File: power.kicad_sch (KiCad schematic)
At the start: 28 parts, among them J3 USB_C_Receptacle_Molex, U11 TPD1E05U06DPY, U4 TPS7A5201QRGRRQ1, U6 TPS7A5201QRGRRQ1

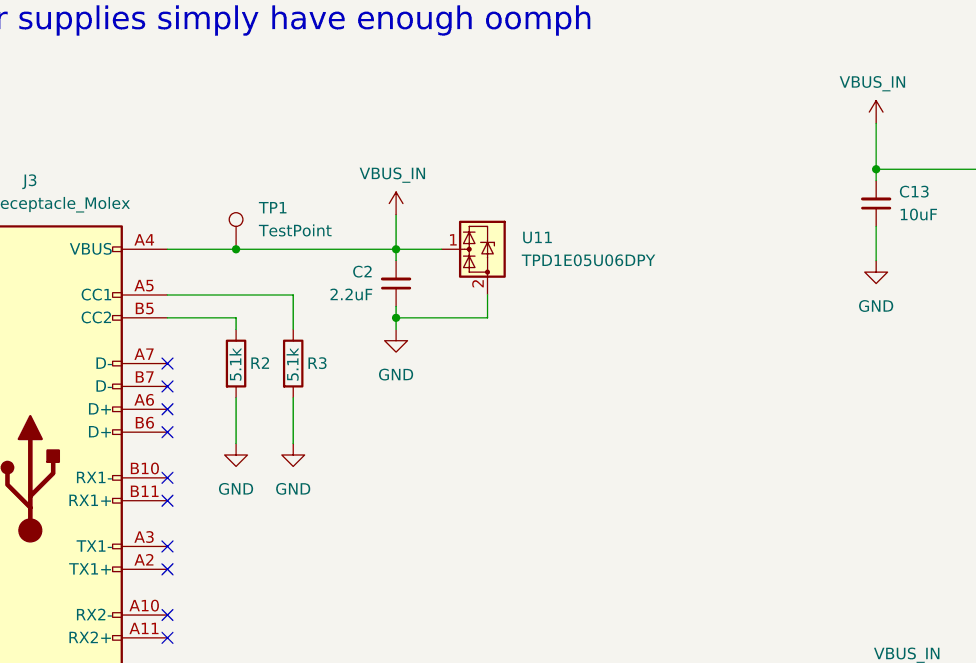
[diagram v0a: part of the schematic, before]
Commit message: Start wiring up Pi Pico
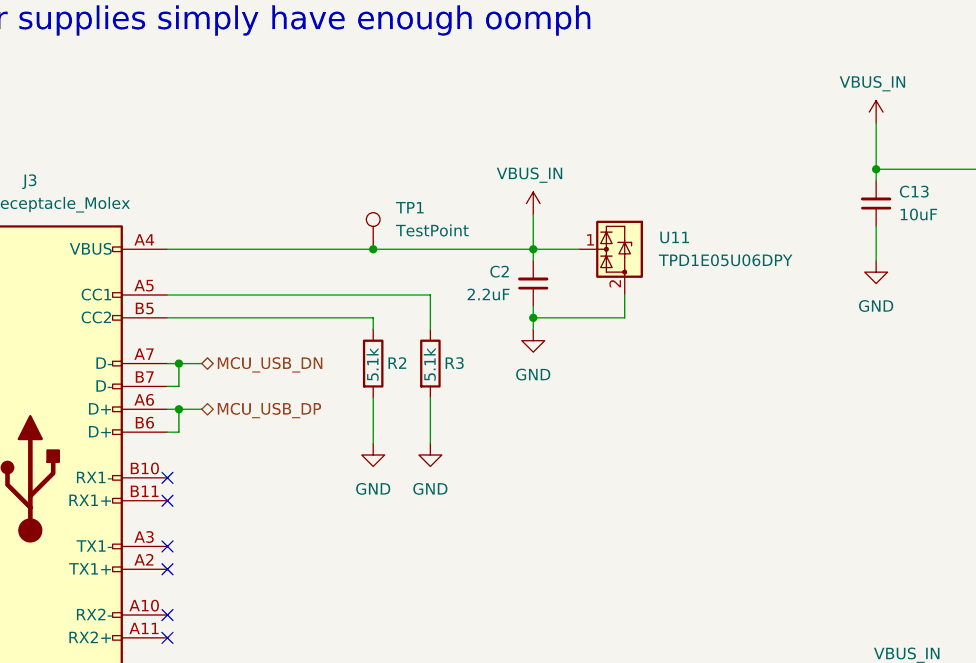
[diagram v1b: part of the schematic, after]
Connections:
- net MCU_USB_DP: now reaches J3.A6 (D+)
- net MCU_USB_DP: now also J3.B6 (D+)
- net MCU_USB_DN: now reaches J3.A7 (D-)
- net MCU_USB_DN: now also J3.B7 (D-)
- no-connect marks 16 -> 12
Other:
- moved on the sheet: C2, R2, R3, TP1, U11

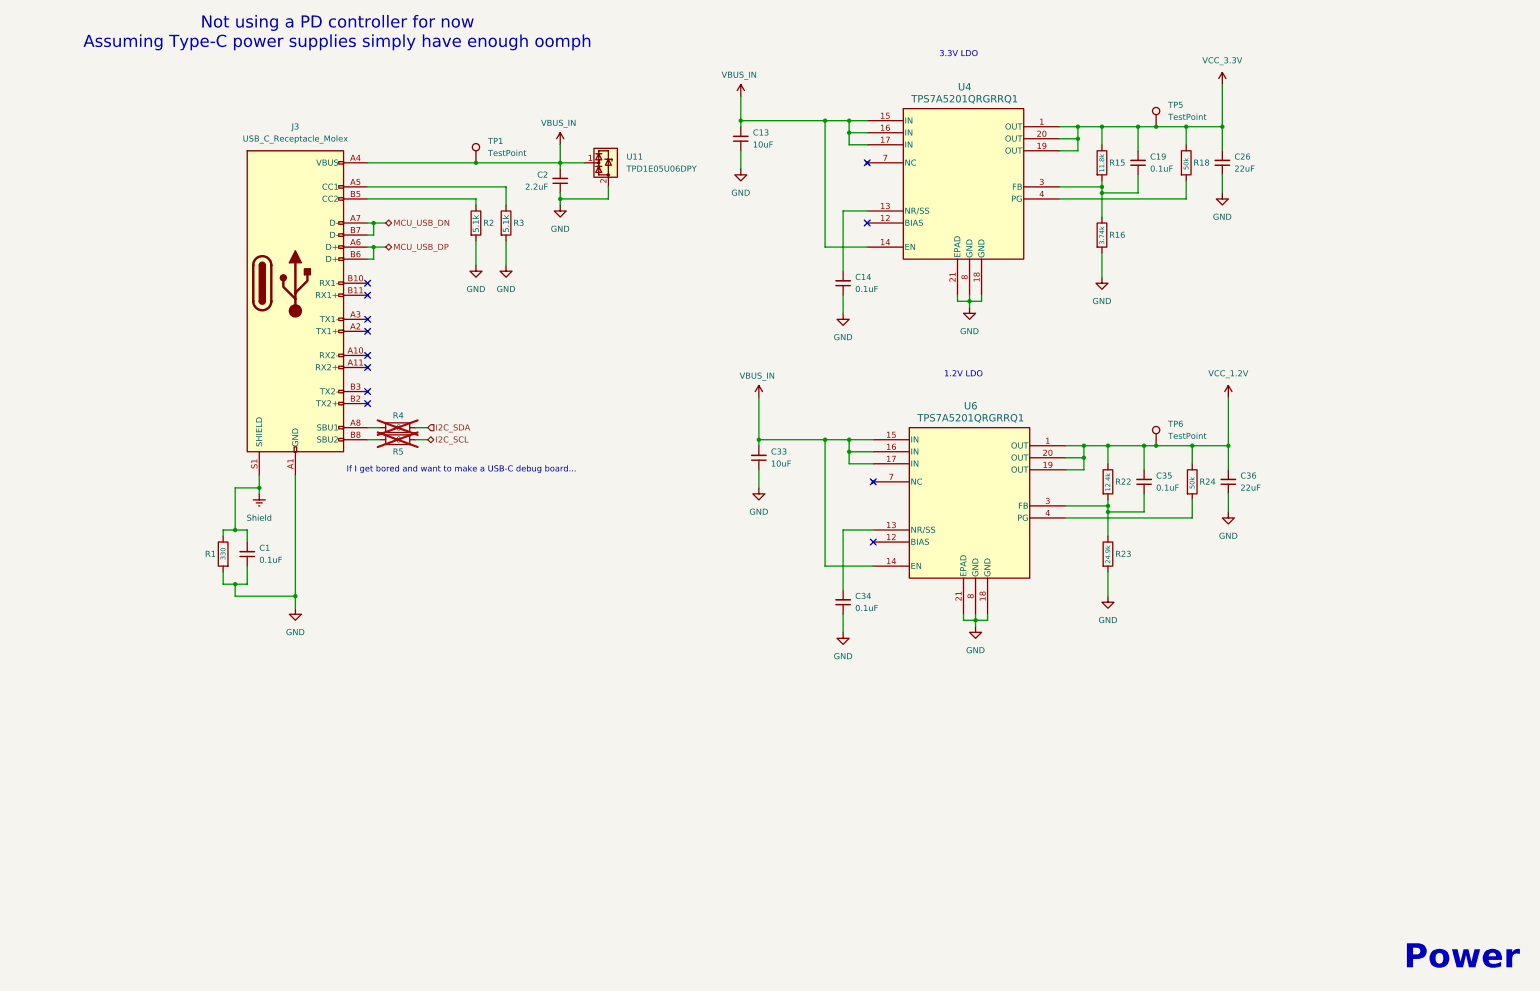
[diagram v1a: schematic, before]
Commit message: Wire up more of the Pico
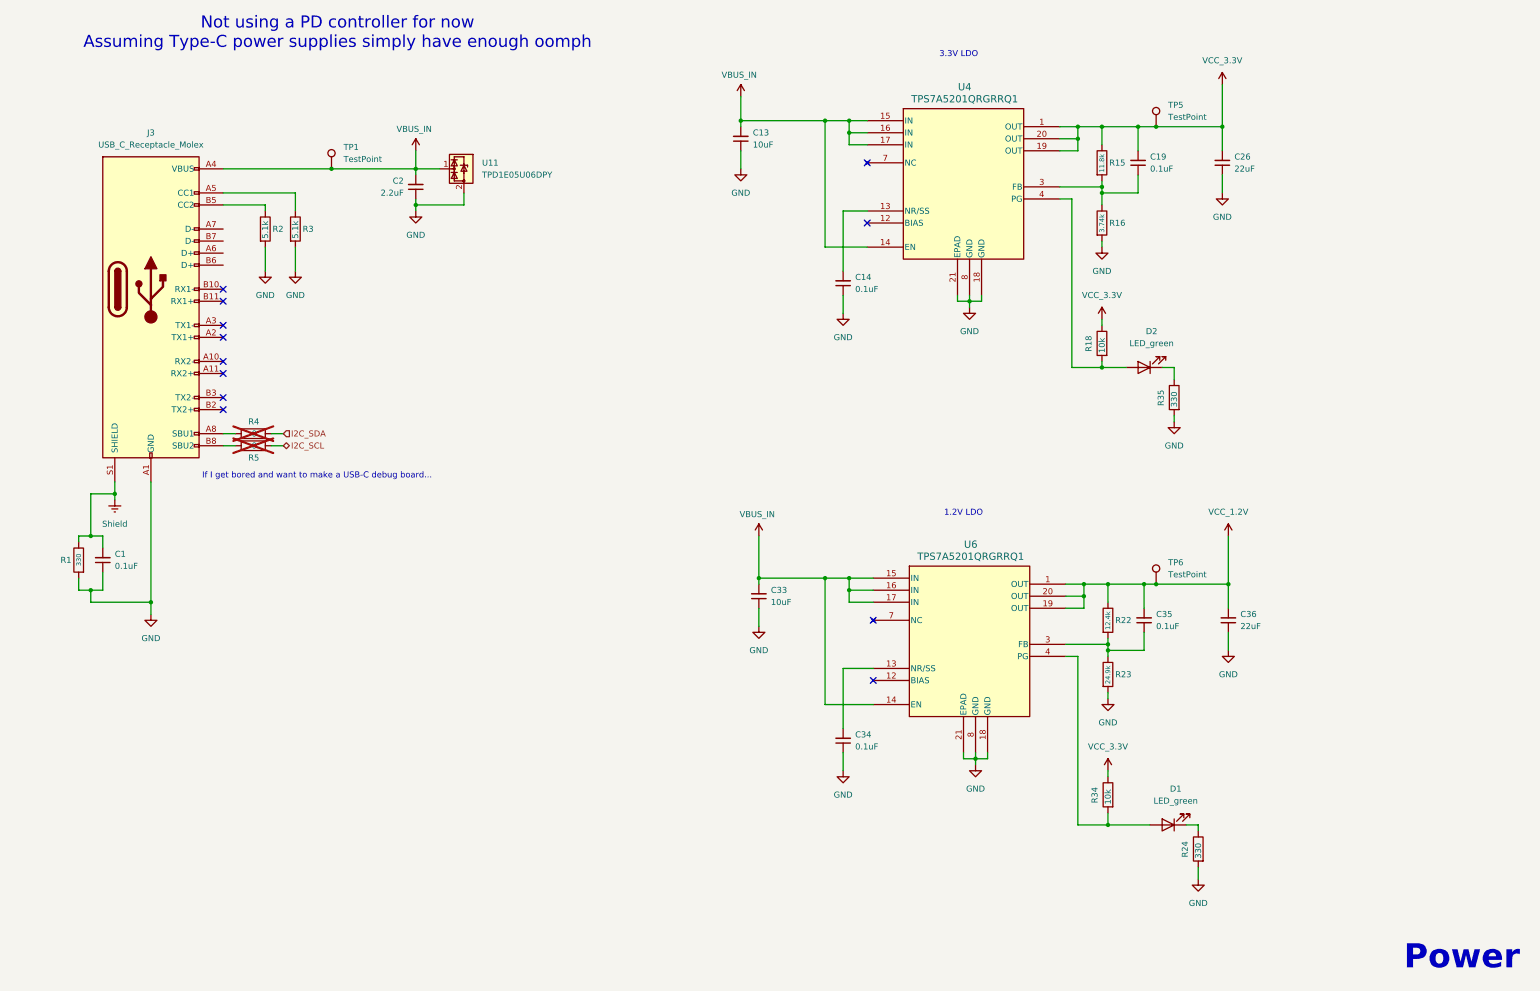
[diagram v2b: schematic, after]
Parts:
- added D1, D2: LED_green, LED_SMD:LED_0603_1608Metric, symbol hubble:LED_green
- added R34: 10k, Resistor_SMD:R_0603_1608Metric, symbol Device:R
- added R35: 330, Resistor_SMD:R_0603_1608Metric, symbol Device:R
- R18: value 50k -> 10k
- R24: value 50k -> 330
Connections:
- net GND: now also R24.2, R35.2
- net VCC_1.2V: no longer R24.1
- net VCC_3.3V: now also R34.1
- net at R18.2, U4.4 (PG): now also D2.2 (A)
- net at U6.4 (PG): now also D1.2 (A), R34.2; no longer R24.2
- net MCU_USB_DN: no longer names the net of J3.A7 (D-)
- net MCU_USB_DN: no longer J3.B7 (D-)
- net MCU_USB_DP: no longer names the net of J3.A6 (D+)
- net MCU_USB_DP: no longer J3.B6 (D+)
- new net: D1.1 (K), R24.1
- new net: D2.1 (K), R35.1
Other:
- moved on the sheet: C1, C2, C33, C34, C35, C36, J3, R1, R16, R2, R22, R23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
